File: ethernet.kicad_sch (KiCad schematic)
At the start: 48 parts, among them J401 Bus_RJ45_5-2337992-8, Q401 PJE138K, U401 TPS2372-3RGWR, U402 ACPL-217-500E, U403 ULS-12_5-D48N-C

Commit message: [#63565] Synchronize components with library, bump revision to 1.0.4
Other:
- company: Antmicro -> Antmicro Ltd
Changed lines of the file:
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@@
   (title_block
     (title "CM4 Baseboard")
-    (date "2024-06-19")
-    (rev "1.0.3")
-    (company "Antmicro")
+    (date "2024-08-02")
+    (rev "1.0.5")
+    (company "Antmicro Ltd")
     (comment 1 "www.antmicro.com")
   )

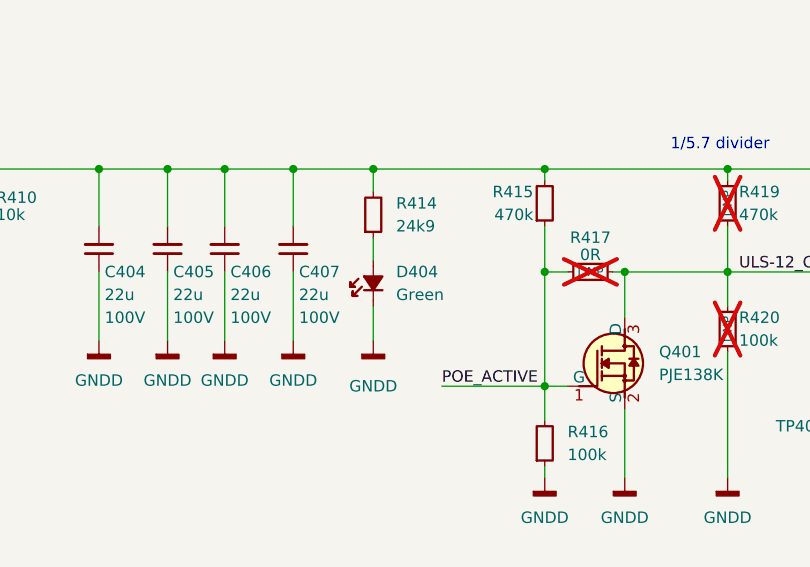
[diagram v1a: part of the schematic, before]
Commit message: [#65638] Fix green LEDs, bump revision to 1.0.5
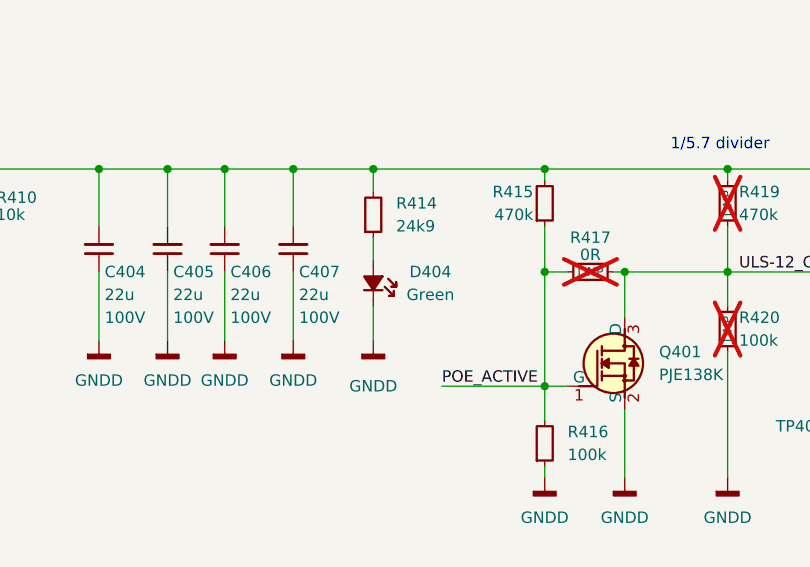
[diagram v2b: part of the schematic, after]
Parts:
- removed D404: LED_G_0603_598-8D80-107F, antmicro-footprints:LED_0603_1608Metric_G, symbol antmicroLEDIndicationDiscrete:LED_G_0603_598-8D80-107F
- added D404: LED_G_0603_KP-1608CGCK, antmicro-footprints:LED_0603_1608Metric_G, symbol antmicroLEDIndicationDiscrete:LED_G_0603_KP-1608CGCK
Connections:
- net GNDD: now also D404.1 (C)
- net at R414.1: now also D404.2 (A)
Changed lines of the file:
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@@
   (title_block
     (title "CM4 Baseboard")
-    (date "2024-08-02")
+    (date "2024-09-12")
     (rev "1.0.5")
     (company "Antmicro Ltd")
@@
     (effects (font (size 1.27 1.27) bold) (justify right))
   )
+  (symbol (lib_id "antmicroLEDIndicationDiscrete:LED_G_0603_KP-1608CGCK") (at 247.65 198.12 270) (mirror x) (unit 1)
+    (in_bom yes) (on_board yes) (dnp no)
+    (property "Reference" "D404" (at 254 194.31 90)
+      (effects (font (size 1.27 1.27) (thickness 0.15)))
+    )
+    (property "Value" "LED_G_0603_KP-1608CGCK" (at 240.03 175.26 0)
+      (effects (font (size 1.27 1.27) (thickness 0.15)) (justify left bottom) hide)
+    )
+    (property "Footprint" "antmicro-footprints:LED_0603_1608Metric_G" (at 237.49 175.26 0)
+      (effects (font (size 1.27 1.27) (thickness 0.15)) (justify left bottom) hide)
+    )
+    (property "Datasheet" "http://www.kingbright.com/attachments/file/psearch//000/00/00/KP-1608CGCK(Ver.23B).pdf" (at 234.95 175.26 0)
+      (effects (font (size 1.27 1.27) (thickness 0.15)) (justify left bottom) hide)
+    )
+    (property "MPN" "KP-1608CGCK" (at 232.41 175.26 0)
+      (effects (font (size 1.27 1.27) (thickness 0.15)) (justify left bottom) hide)
+    )
+    (property "Manufacturer" "Kingbright" (at 229.87 175.26 0)
+      (effects (font (size 1.27 1.27) (thickness 0.15)) (justify left bottom) hide)
+    )
+    (property "Color" "Green" (at 254 196.85 90)
+      (effects (font (size 1.27 1.27)))
+    )
+    (property "Author" "Antmicro" (at 227.33 175.26 0)
+      (effects (font (size 1.27 1.27) (thickness 0.15)) (justify left bottom) hide)
+    )
+    (property "License" "Apache-2.0" (at 224.79 175.26 0)
+      (effects (font (size 1.27 1.27) (thickness 0.15)) (justify left bottom) hide)
+    )
+    (pin "2")
+    (pin "1")
+    (instances
+      (project "cm4-baseboard"
+        (path "/60b842dc-0853-4a25-99ac-5784ddf94d0d/00000000-0000-0000-0000-00005fea17d8"
+          (reference "D404") (unit 1)
+        )
+      )
+    )
+  )
   (symbol (lib_id "antmicropower:PWR_FLAG") (at 137.16 181.61 0) (unit 1)
     (in_bom yes) (on_board yes) (dnp no)
@@
         )
       )
-    )
-  )
-  (symbol (lib_id "antmicroLEDIndicationDiscrete:LED_G_0603_598-8D80-107F") (at 247.65 198.12 90) (unit 1)
-    (in_bom yes) (on_board yes) (dnp no) (fields_autoplaced)
-    (property "Reference" "D404" (at 250.19 194.31 90)
-      (effects (font (size 1.27 1.27) (thickness 0.15)) (justify right))
-    )
-    (property "Value" "LED_G_0603_598-8D80-107F" (at 255.27 175.26 0)
-      (effects (font (size 1.27 1.27) (thickness 0.15)) (justify left bottom) hide)
-    )
-    (property "Footprint" "antmicro-footprints:LED_0603_1608Metric_G" (at 257.81 175.26 0)
-      (effects (font (size 1.27 1.27) (thickness 0.15)) (justify left bottom) hide)
-    )
-    (property "Datasheet" "https://www.dialight.com/wp-content/uploads/2021/07/DIA_Selector_Guide_SMD_042321.pdf" (at 260.35 175.26 0)
-      (effects (font (size 1.27 1.27) (thickness 0.15)) (justify left bottom) hide)
-    )
-    (property "MPN" "598-8D80-107F" (at 262.89 175.26 0)
-      (effects (font (size 1.27 1.27) (thickness 0.15)) (justify left bottom) hide)
-    )
-    (property "Manufacturer" "Dialight" (at 265.43 175.26 0)
-      (effects (font (size 1.27 1.27) (thickness 0.15)) (justify left bottom) hide)
-    )
-    (property "Author" "Antmicro" (at 267.97 175.26 0)
-      (effects (font (size 1.27 1.27) (thickness 0.15)) (justify left bottom) hide)
-    )
-    (property "License" "Apache-2.0" (at 270.51 175.26 0)
-      (effects (font (size 1.27 1.27) (thickness 0.15)) (justify left bottom) hide)
-    )
-    (property "Color" "Green" (at 250.19 196.85 90)
-      (effects (font (size 1.27 1.27)) (justify right))
-    )
-    (pin "1")
-    (pin "2")
-    (instances
-      (project "cm4-baseboard"
-        (path "/60b842dc-0853-4a25-99ac-5784ddf94d0d/00000000-0000-0000-0000-00005fea17d8"
-          (reference "D404") (unit 1)
-        )
-      )
